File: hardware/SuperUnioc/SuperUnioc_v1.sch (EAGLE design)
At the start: 71 parts, among them IC1 MAX3232CSE, IC2 ADXRS453BRGZ, IC5 XMEGA128-A1

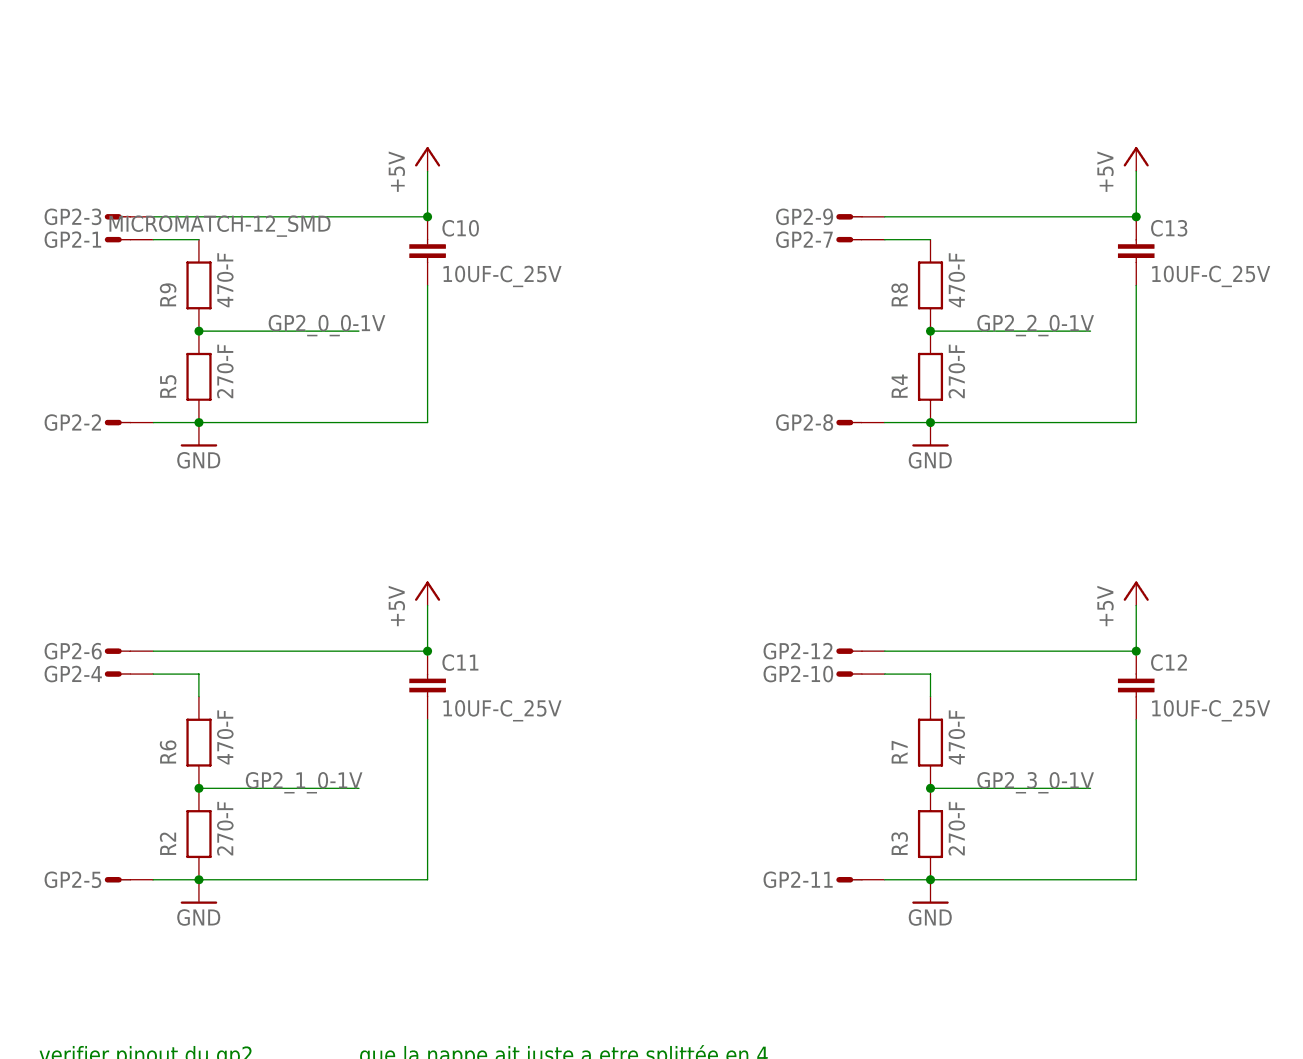
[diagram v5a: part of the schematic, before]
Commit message: corrected adxrs453 footrpint and gp2 connector footprint
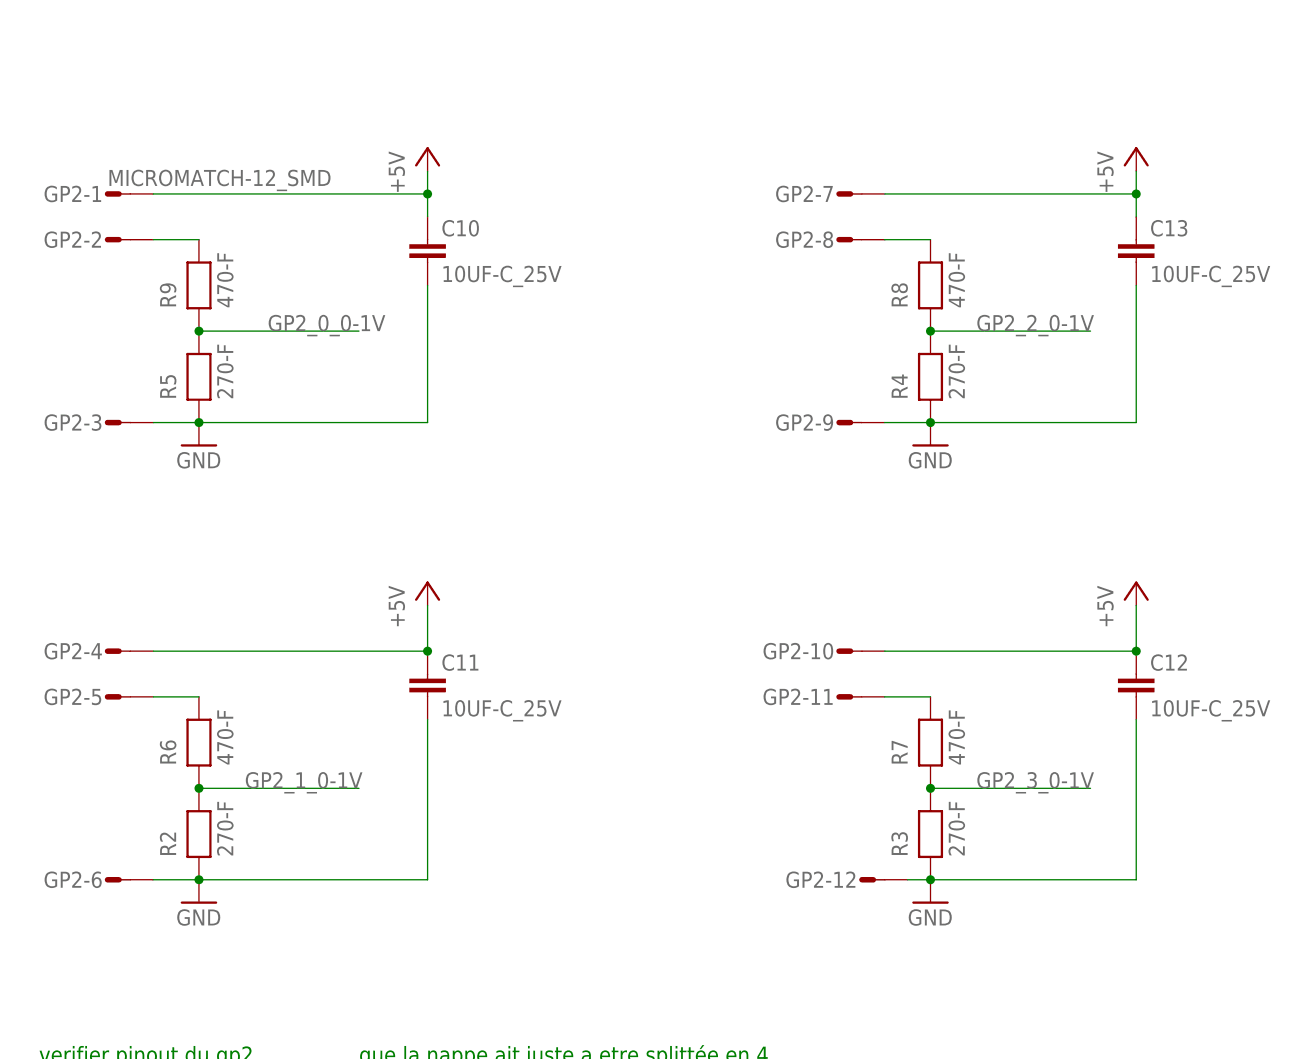
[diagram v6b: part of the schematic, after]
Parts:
- IC2: device robotter_ic:ADXRS453BRGZ -> robotter_ic:ADXRS453BRG
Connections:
- net +5V: now also GP2-1.S, GP2-10.S, GP2-4.S, GP2-7.S; no longer GP2-12.S, GP2-3.S, GP2-6.S, GP2-9.S
- net GND: now also GP2-12.S, GP2-3.S, GP2-6.S, GP2-9.S; no longer GP2-11.S, GP2-2.S, GP2-5.S, GP2-8.S
- net N$22: now also GP2-8.S, R8.2; no longer GP2-1.S, R9.2
- net N$24: now also GP2-2.S, R9.2; no longer GP2-7.S, R8.2
- net N$36: now also GP2-11.S; no longer GP2-10.S
- net N$37: now also GP2-5.S; no longer GP2-4.S
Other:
- moved on the sheet: GP2-1, GP2-10, GP2-11, GP2-12, GP2-2, GP2-3, GP2-4, GP2-5, GP2-6, GP2-7, GP2-8, GP2-9
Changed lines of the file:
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@@
 <part name="+3V24" library="supply1" deviceset="+3V3" device=""/>
 <part name="GND8" library="supply1" deviceset="GND" device=""/>
-<part name="IC2" library="robotter_ic" deviceset="ADXRS453" device="BRGZ" value="ADXRS453BRGZ"/>
+<part name="IC2" library="robotter_ic" deviceset="ADXRS453" device="BRG" value="ADXRS453BRGZ"/>
 <part name="+3V4" library="supply1" deviceset="+3V3" device=""/>
 <part name="+3V7" library="supply1" deviceset="+3V3" device=""/>
@@
 <instance part="H5" gate="G$1" x="187.96" y="43.18" rot="R90"/>
 <instance part="FRAME5" gate="G$1" x="0" y="-185.42"/>
-<instance part="GP2" gate="-1" x="33.02" y="-43.18"/>
-<instance part="GP2" gate="-2" x="33.02" y="-63.5"/>
-<instance part="GP2" gate="-3" x="33.02" y="-40.64"/>
-<instance part="GP2" gate="-4" x="33.02" y="-91.44"/>
-<instance part="GP2" gate="-5" x="33.02" y="-114.3"/>
-<instance part="GP2" gate="-6" x="33.02" y="-88.9"/>
-<instance part="GP2" gate="-7" x="114.3" y="-43.18"/>
-<instance part="GP2" gate="-8" x="114.3" y="-63.5"/>
-<instance part="GP2" gate="-9" x="114.3" y="-40.64"/>
-<instance part="GP2" gate="-10" x="114.3" y="-91.44"/>
-<instance part="GP2" gate="-11" x="114.3" y="-114.3"/>
-<instance part="GP2" gate="-12" x="114.3" y="-88.9"/>
+<instance part="GP2" gate="-1" x="33.02" y="-38.1"/>
+<instance part="GP2" gate="-2" x="33.02" y="-43.18"/>
+<instance part="GP2" gate="-3" x="33.02" y="-63.5"/>
+<instance part="GP2" gate="-4" x="33.02" y="-88.9"/>
+<instance part="GP2" gate="-5" x="33.02" y="-93.98"/>
+<instance part="GP2" gate="-6" x="33.02" y="-114.3"/>
+<instance part="GP2" gate="-7" x="114.3" y="-38.1"/>
+<instance part="GP2" gate="-8" x="114.3" y="-43.18"/>
+<instance part="GP2" gate="-9" x="114.3" y="-63.5"/>
+<instance part="GP2" gate="-10" x="114.3" y="-88.9"/>
+<instance part="GP2" gate="-11" x="114.3" y="-93.98"/>
+<instance part="GP2" gate="-12" x="116.84" y="-114.3"/>
 <instance part="R2" gate="G$1" x="43.18" y="-109.22" rot="R90"/>
 <instance part="R3" gate="G$1" x="124.46" y="-109.22" rot="R90"/>
@@
 <segment>
 <pinref part="R2" gate="G$1" pin="1"/>
-<wire x1="38.1" y1="-114.3" x2="43.18" y2="-114.3" width="0.1524" layer="91"/>
 <wire x1="68.58" y1="-96.52" x2="68.58" y2="-114.3" width="0.1524" layer="91"/>
 <wire x1="68.58" y1="-114.3" x2="43.18" y2="-114.3" width="0.1524" layer="91"/>
@@
 <junction x="43.18" y="-114.3"/>
 <pinref part="C11" gate="G$1" pin="2"/>
-<pinref part="GP2" gate="-5" pin="S"/>
+<pinref part="GP2" gate="-6" pin="S"/>
+<wire x1="38.1" y1="-114.3" x2="43.18" y2="-114.3" width="0.1524" layer="91"/>
 </segment>
 <segment>
 <pinref part="R3" gate="G$1" pin="1"/>
-<wire x1="119.38" y1="-114.3" x2="124.46" y2="-114.3" width="0.1524" layer="91"/>
 <wire x1="147.32" y1="-96.52" x2="147.32" y2="-114.3" width="0.1524" layer="91"/>
 <wire x1="147.32" y1="-114.3" x2="124.46" y2="-114.3" width="0.1524" layer="91"/>
@@
 <junction x="124.46" y="-114.3"/>
 <pinref part="C12" gate="G$1" pin="2"/>
-<pinref part="GP2" gate="-11" pin="S"/>
+<pinref part="GP2" gate="-12" pin="S"/>
+<wire x1="121.92" y1="-114.3" x2="124.46" y2="-114.3" width="0.1524" layer="91"/>
 </segment>
 <segment>
 <pinref part="R4" gate="G$1" pin="1"/>
-<wire x1="119.38" y1="-63.5" x2="124.46" y2="-63.5" width="0.1524" layer="91"/>
 <wire x1="147.32" y1="-48.26" x2="147.32" y2="-63.5" width="0.1524" layer="91"/>
 <wire x1="147.32" y1="-63.5" x2="124.46" y2="-63.5" width="0.1524" layer="91"/>
@@
 <junction x="124.46" y="-63.5"/>
 <pinref part="C13" gate="G$1" pin="2"/>
-<pinref part="GP2" gate="-8" pin="S"/>
+<pinref part="GP2" gate="-9" pin="S"/>
+<wire x1="119.38" y1="-63.5" x2="124.46" y2="-63.5" width="0.1524" layer="91"/>
 </segment>
 <segment>
@@
 <junction x="43.18" y="-63.5"/>
 <pinref part="C10" gate="G$1" pin="2"/>
-<pinref part="GP2" gate="-2" pin="S"/>
+<pinref part="GP2" gate="-3" pin="S"/>
 <wire x1="38.1" y1="-63.5" x2="43.18" y2="-63.5" width="0.1524" layer="91"/>
 </segment>
@@
 </segment>
 <segment>
-<pinref part="GP2" gate="-6" pin="S"/>
-<wire x1="38.1" y1="-88.9" x2="68.58" y2="-88.9" width="0.1524" layer="91"/>
 <pinref part="P+6" gate="1" pin="+5V"/>
 <wire x1="68.58" y1="-88.9" x2="68.58" y2="-83.82" width="0.1524" layer="91"/>
 <pinref part="C11" gate="G$1" pin="1"/>
+<pinref part="GP2" gate="-4" pin="S"/>
+<wire x1="38.1" y1="-88.9" x2="68.58" y2="-88.9" width="0.1524" layer="91"/>
 <junction x="68.58" y="-88.9"/>
 </segment>
 <segment>
-<pinref part="GP2" gate="-12" pin="S"/>
-<wire x1="119.38" y1="-88.9" x2="147.32" y2="-88.9" width="0.1524" layer="91"/>
 <pinref part="P+5" gate="1" pin="+5V"/>
 <wire x1="147.32" y1="-88.9" x2="147.32" y2="-83.82" width="0.1524" layer="91"/>
 <pinref part="C12" gate="G$1" pin="1"/>
+<pinref part="GP2" gate="-10" pin="S"/>
+<wire x1="119.38" y1="-88.9" x2="147.32" y2="-88.9" width="0.1524" layer="91"/>
 <junction x="147.32" y="-88.9"/>
 </segment>
 <segment>
-<pinref part="GP2" gate="-9" pin="S"/>
-<wire x1="119.38" y1="-40.64" x2="147.32" y2="-40.64" width="0.1524" layer="91"/>
 <pinref part="P+4" gate="1" pin="+5V"/>
-<wire x1="147.32" y1="-40.64" x2="147.32" y2="-35.56" width="0.1524" layer="91"/>
+<wire x1="147.32" y1="-40.64" x2="147.32" y2="-38.1" width="0.1524" layer="91"/>
 <pinref part="C13" gate="G$1" pin="1"/>
-<junction x="147.32" y="-40.64"/>
+<pinref part="GP2" gate="-7" pin="S"/>
+<wire x1="147.32" y1="-38.1" x2="147.32" y2="-35.56" width="0.1524" layer="91"/>
+<wire x1="119.38" y1="-38.1" x2="147.32" y2="-38.1" width="0.1524" layer="91"/>
+<junction x="147.32" y="-38.1"/>
 </segment>
 <segment>
 <pinref part="P+3" gate="1" pin="+5V"/>
-<wire x1="68.58" y1="-40.64" x2="68.58" y2="-35.56" width="0.1524" layer="91"/>
+<wire x1="68.58" y1="-40.64" x2="68.58" y2="-38.1" width="0.1524" layer="91"/>
 <pinref part="C10" gate="G$1" pin="1"/>
-<pinref part="GP2" gate="-3" pin="S"/>
-<wire x1="38.1" y1="-40.64" x2="68.58" y2="-40.64" width="0.1524" layer="91"/>
-<junction x="68.58" y="-40.64"/>
+<pinref part="GP2" gate="-1" pin="S"/>
+<wire x1="68.58" y1="-38.1" x2="68.58" y2="-35.56" width="0.1524" layer="91"/>
+<wire x1="38.1" y1="-38.1" x2="68.58" y2="-38.1" width="0.1524" layer="91"/>
+<junction x="68.58" y="-38.1"/>
 </segment>
 </net>
@@
 <segment>
 <pinref part="R7" gate="G$1" pin="2"/>
-<wire x1="124.46" y1="-93.98" x2="124.46" y2="-91.44" width="0.1524" layer="91"/>
-<pinref part="GP2" gate="-10" pin="S"/>
-<wire x1="119.38" y1="-91.44" x2="124.46" y2="-91.44" width="0.1524" layer="91"/>
+<wire x1="124.46" y1="-93.98" x2="119.38" y2="-93.98" width="0.1524" layer="91"/>
+<pinref part="GP2" gate="-11" pin="S"/>
 </segment>
 </net>
@@
 <segment>
 <pinref part="R6" gate="G$1" pin="2"/>
-<wire x1="43.18" y1="-93.98" x2="43.18" y2="-91.44" width="0.1524" layer="91"/>
-<pinref part="GP2" gate="-4" pin="S"/>
-<wire x1="38.1" y1="-91.44" x2="43.18" y2="-91.44" width="0.1524" layer="91"/>
-</segment>
-</net>
-<net name="N$22" class="0">
-<segment>
-<pinref part="R9" gate="G$1" pin="2"/>
-<pinref part="GP2" gate="-1" pin="S"/>
-<wire x1="38.1" y1="-43.18" x2="43.18" y2="-43.18" width="0.1524" layer="91"/>
-</segment>
-</net>
-<net name="N$24" class="0">
-<segment>
-<pinref part="GP2" gate="-7" pin="S"/>
-<pinref part="R8" gate="G$1" pin="2"/>
-<wire x1="119.38" y1="-43.18" x2="124.46" y2="-43.18" width="0.1524" layer="91"/>
+<wire x1="43.18" y1="-93.98" x2="38.1" y2="-93.98" width="0.1524" layer="91"/>
+<pinref part="GP2" gate="-5" pin="S"/>
 </segment>
 </net>
@@
 </segment>
 </net>
+<net name="N$22" class="0">
+<segment>
+<pinref part="R8" gate="G$1" pin="2"/>
+<pinref part="GP2" gate="-8" pin="S"/>
+<wire x1="119.38" y1="-43.18" x2="124.46" y2="-43.18" width="0.1524" layer="91"/>
+</segment>
+</net>
+<net name="N$24" class="0">
+<segment>
+<pinref part="R9" gate="G$1" pin="2"/>
+<pinref part="GP2" gate="-2" pin="S"/>
+<wire x1="38.1" y1="-43.18" x2="43.18" y2="-43.18" width="0.1524" layer="91"/>
+</segment>
+</net>
